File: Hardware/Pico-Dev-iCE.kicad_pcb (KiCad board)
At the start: 4 copper layers, 100 x 100 mm, 294 parts, among them J10 SDR ANT, J11 Conn_01x20_Socket, J12 Conn_01x20_Socket, J2 S11, J4 S21, J5 AWG_OUT, J6 PMOD, J7 Conn_01x02, J8 OLED, J9 3.5mm_Jack, Q1 2N7002, Q2 2N7002, Q3 AO3401A, Q4 2N7002, Q5 2N7002, Q6 2N7002, Q7 2N7002, Q8 2N7002, Q9 2N7002, SW1 RotaryEncoder_Switch_MP, U1 74LVC1G3157GW, U10 PAM8908, U11 NCP115AMX120TCG, U12 74LVC1G3157GW, U13 TPH2501-TR, U14 74LVC1G3157GW, U15 74LVC1G3157GW, U16 74LVC1G3157GW, U17 74LVC1G3157GW, U18 74LVC1G3157GW, U19 74LVC1G3157GW, U2 TPH2501-TR, U20 TPH2501-TR, U21 74LVC1G3157GW, U22 74LVC1G3157GW, U23 74LVC1G3157GW, U24 74LVC1G3157GW, U3 TPH2501-TR, U4 MS9280, U5 MS9708, U6 74LVC1G3157GW, U7 ICE40UP5K-SG48ITR, U8 L78M05ABDT-TR, U9 CJC4334H, X1 SG-8018CE 30.720000MHz TJHPA

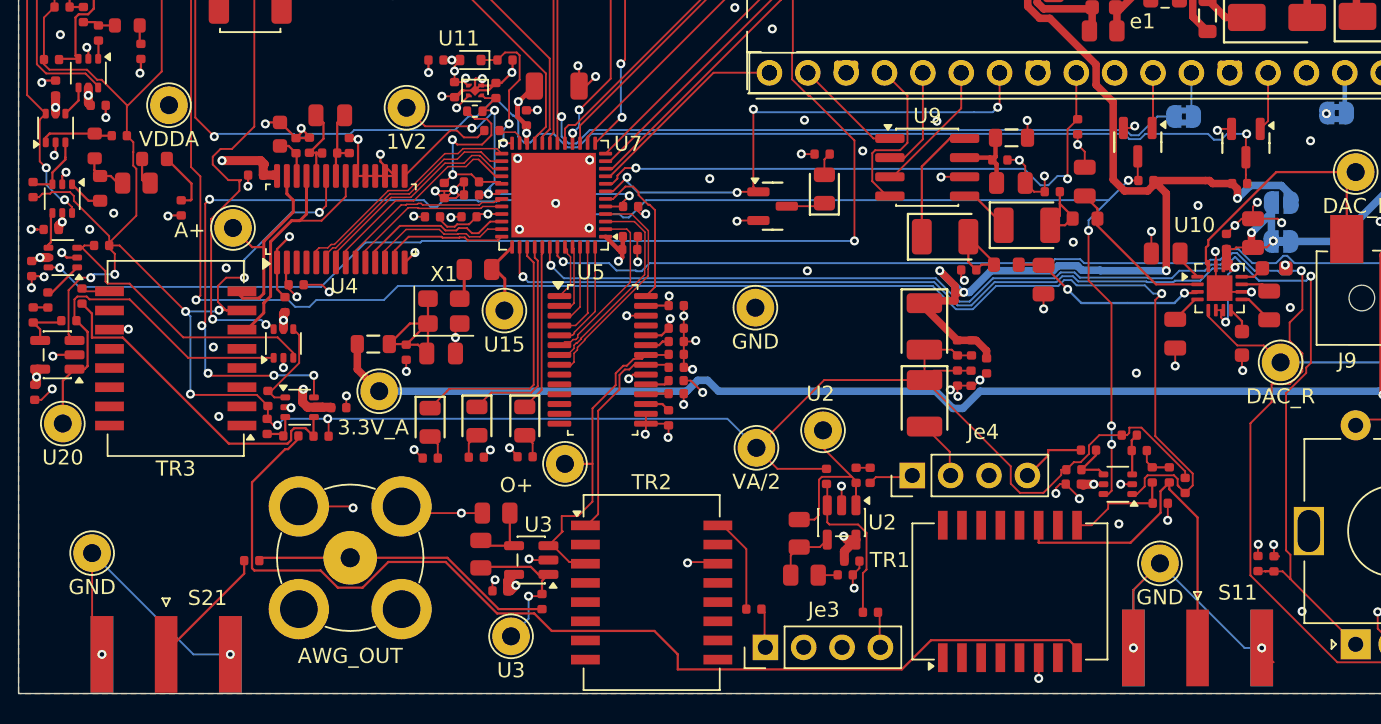
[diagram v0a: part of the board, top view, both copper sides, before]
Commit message: fixed U4 ad SMA footprints
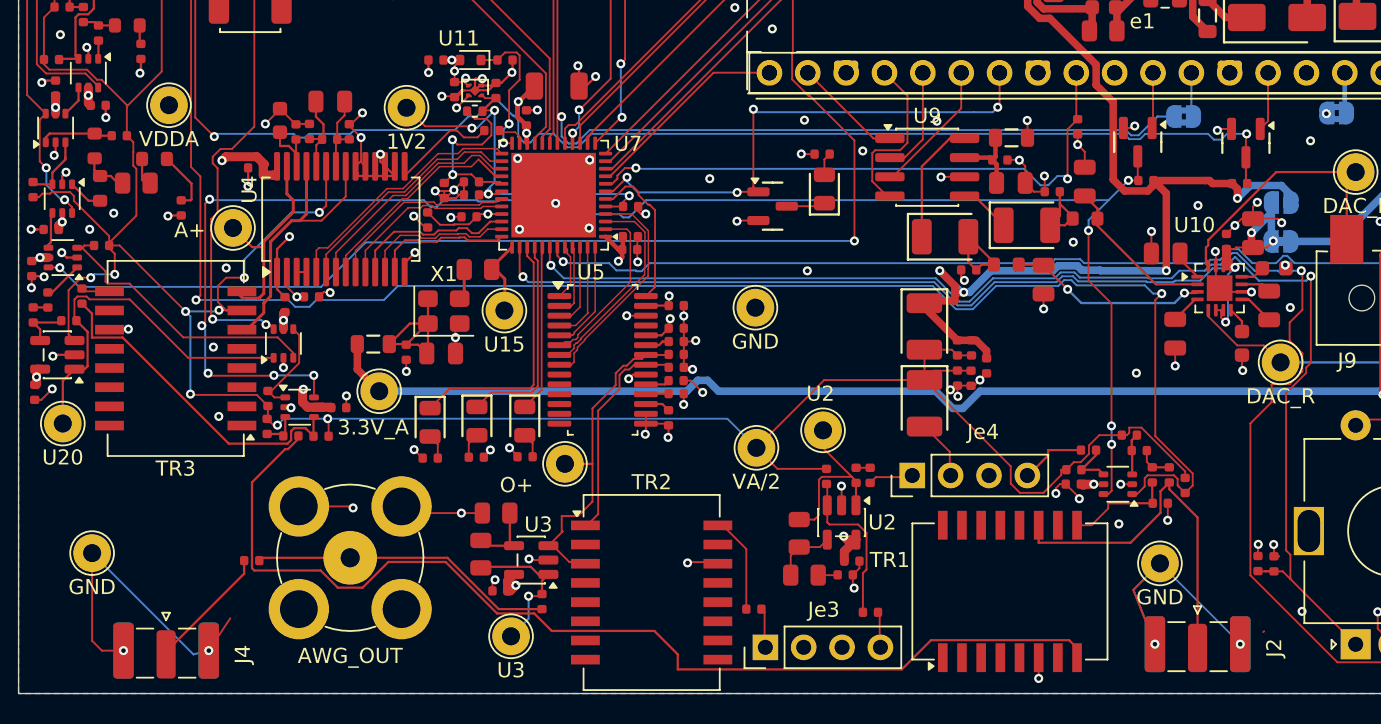
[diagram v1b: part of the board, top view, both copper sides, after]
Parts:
- J2, J4: footprint Connector_Coaxial:SMA_Amphenol_132289_EdgeMount -> Connector_Coaxial:SMA_Samtec_SMA-J-P-H-ST-EM1_EdgeMount
- U4: footprint Package_SO:TSSOP-28-1EP_4.4x9.7mm_P0.65mm_EP3.4x9.7mm_Mask3.1x4.05mm_ThermalVias -> Package_SO:SSOP-28_5.3x10.2mm_P0.65mm
- moved C22 1.30 mm to (119.4, 123.7)
- moved C10 0.91 mm to (120.6, 113.3)
- moved C11 0.91 mm to (119.3, 112.8)
- moved C12 0.91 mm to (117.3, 112.0)
- moved C16 0.91 mm to (120.6, 110.8)
- moved C17 0.91 mm to (118.4, 112.8)
- moved C8 0.91 mm to (121.9, 112.8)
- moved C20 0.48 mm to (115.7, 115.2)
- moved C37 0.38 mm to (127.1, 118.6), turned to -90 degrees
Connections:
- A1 pad 30: unconnected-(A1-RUN-Pad30) -> /30
- A1 pad 35: unconnected-(A1-ADC_VREF-Pad35) -> /35
- A1 pad 37: unconnected-(A1-3V3_EN-Pad37) -> /37
- J12 pad 30: unconnected-(J12-Pin_11-Pad30) -> /30
- J12 pad 35: unconnected-(J12-Pin_6-Pad35) -> /35
- J12 pad 37: unconnected-(J12-Pin_4-Pad37) -> /37
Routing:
- net Net-(U4-VREF): track 2.78 -> 5.49 mm
- net +3V3: track 37.4 -> 39.4 mm
- net Net-(U4-REFTF): track 5.06 -> 6.88 mm
- net Net-(Q7-D): track 174.3 -> 172.5 mm
- net Net-(U4-REFBF): track 5.46 -> 6.99 mm
- net (no net): track 0.00 -> 0.65 mm
- net /D6: track 10.5 -> 11.0 mm
